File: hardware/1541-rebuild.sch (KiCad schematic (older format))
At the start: 1 part

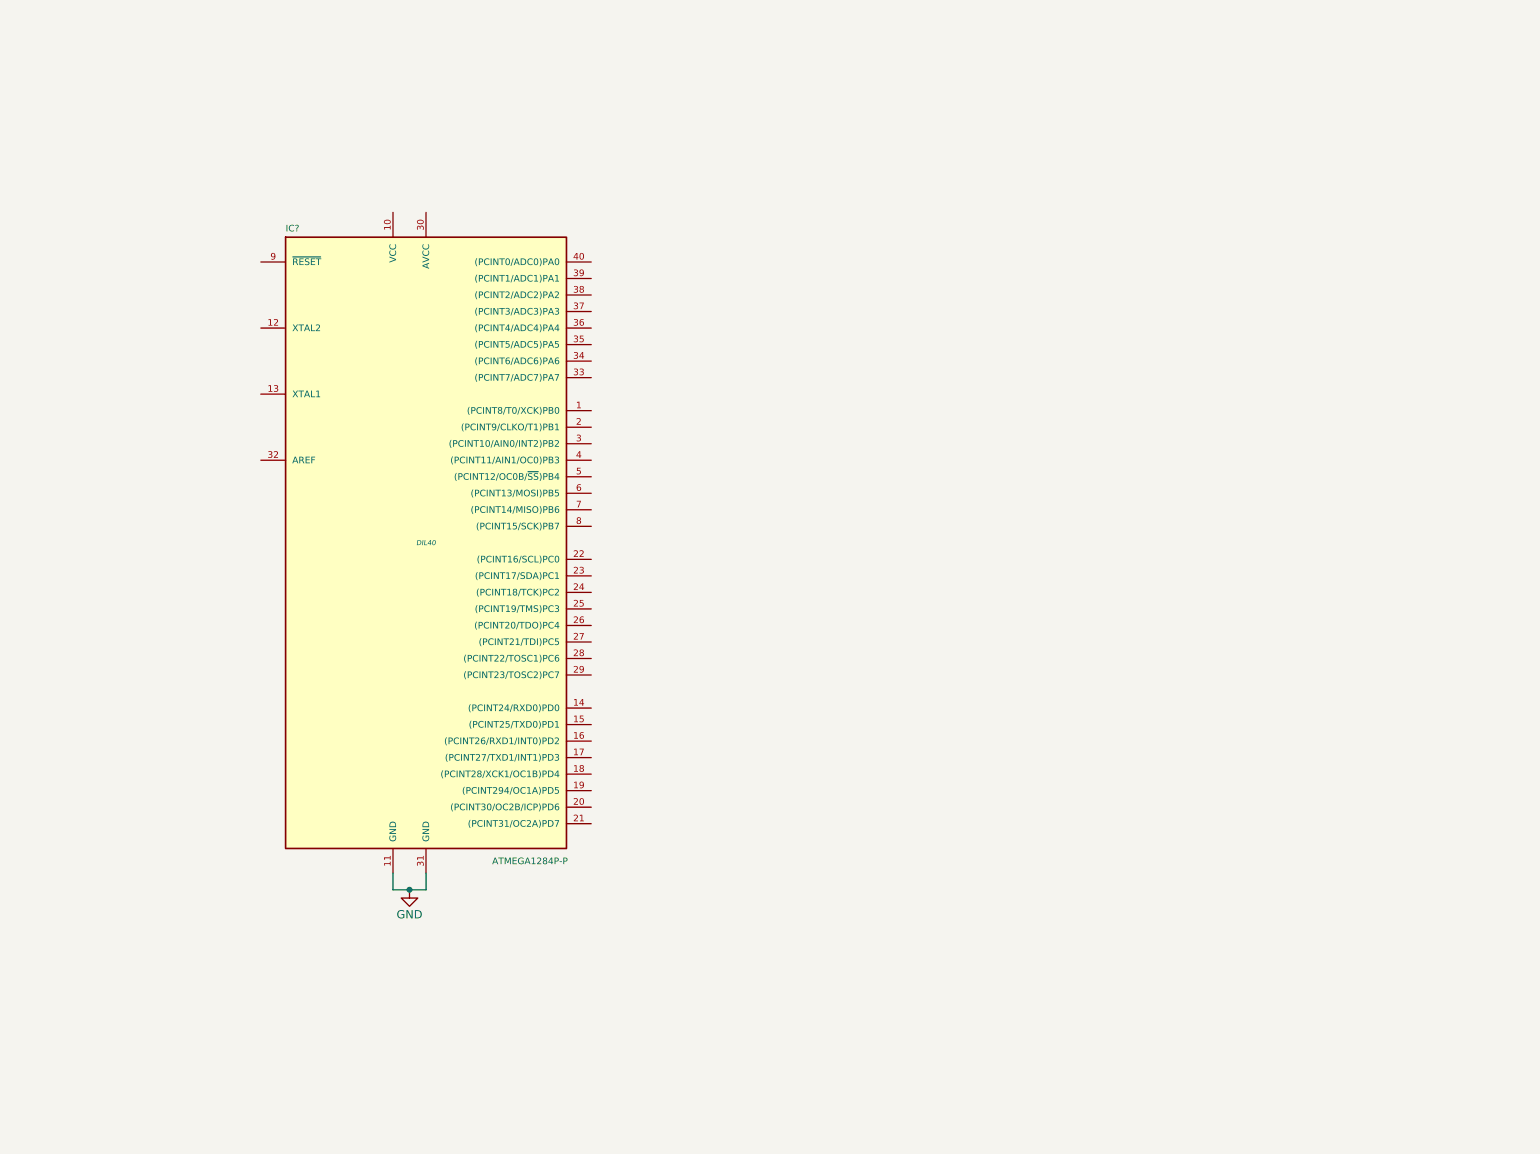
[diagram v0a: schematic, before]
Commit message: Im Schaltplan die SD Karten Anbindung eingefügt
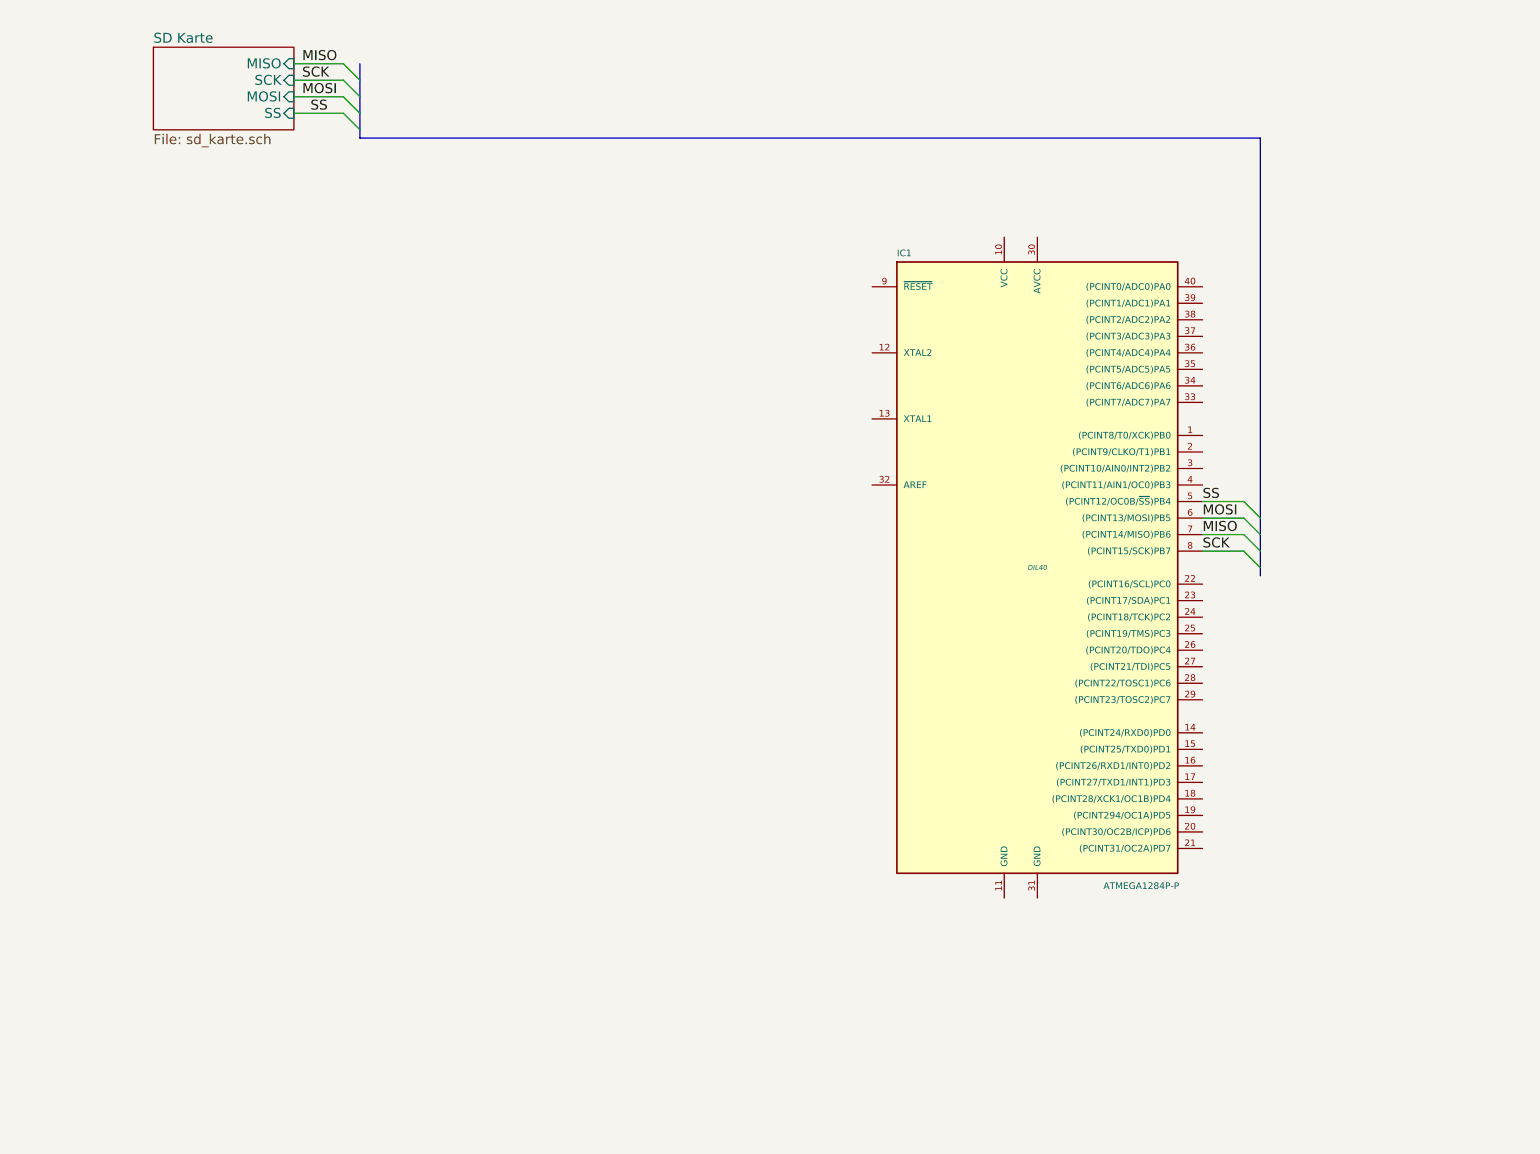
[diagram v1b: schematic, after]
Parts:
- removed IC?: ATMEGA1284P-P, DIL40, symbol ATMEGA1284P-P
- added IC1: ATMEGA1284P-P, DIL40, symbol ATMEGA1284P-P
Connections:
- new net MISO: IC1.7 ((PCINT14/MISO)PB6)
- new net MOSI: IC1.6 ((PCINT13/MOSI)PB5)
- new net SCK: IC1.8 ((PCINT15/SCK)PB7)
- new net SS: IC1.5 ((PCINT12/OC0B/~SS~)PB4)
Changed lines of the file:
@@
 LIBS:contrib
 LIBS:valves
+LIBS:1541-rebuild-cache
 EELAYER 25 0
 EELAYER END
 $Descr A4 11693 8268
 encoding utf-8
-Sheet 1 1
-Title ""
-Date ""
-Rev ""
+Sheet 1 2
+Title "1541-rebuild"
+Date "2015-09-15"
+Rev "1.0"
 Comp ""
-Comment1 ""
+Comment1 "Erstellt: von: Thorsten Kattanek"
 Comment2 ""
 Comment3 ""
 Comment4 ""
 $EndDescr
+$Sheet
+S 1500 850  850  500
+U 55F7A0F9
+F0 "SD Karte" 60
+F1 "sd_karte.sch" 60
+F2 "MISO" I R 2350 950 60
+F3 "SCK" I R 2350 1050 60
+F4 "MOSI" I R 2350 1150 60
+F5 "SS" I R 2350 1250 60
+$EndSheet
 $Comp
-L ATMEGA1284P-P IC?
-U 1 1 55F6F7E1
-P 3150 3850
-F 0 "IC?" H 2300 5730 40  0000 L BNN
-F 1 "ATMEGA1284P-P" H 3550 1900 40  0000 L BNN
-F 2 "DIL40" H 3150 3850 30  0000 C CIN
-F 3 "" H 3150 3850 60  0000 C CNN
-	1    3150 3850
+L ATMEGA1284P-P IC1
+U 1 1 55F7E447
+P 6850 4000
+F 0 "IC1" H 6000 5880 40  0000 L BNN
+F 1 "ATMEGA1284P-P" H 7250 2050 40  0000 L BNN
+F 2 "DIL40" H 6850 4000 30  0000 C CIN
+F 3 "" H 6850 4000 60  0000 C CNN
+	1    6850 4000
 	1    0    0    -1
 $EndComp
-$Comp
-L GND #PWR?
-U 1 1 55F6F9CF
-P 3050 5950
-F 0 "#PWR?" H 3050 5700 50  0001 C CNN
-F 1 "GND" H 3050 5800 50  0000 C CNN
-F 2 "" H 3050 5950 60  0000 C CNN
-F 3 "" H 3050 5950 60  0000 C CNN
-	1    3050 5950
-	1    0    0    -1
-$EndComp
+Wire Bus Line
+	2750 950  2750 1400
+Wire Bus Line
+	2750 1400 8200 1400
+Wire Bus Line
+	8200 1400 8200 4050
+Entry Wire Line
+	2650 950  2750 1050
+Entry Wire Line
+	2650 1050 2750 1150
+Entry Wire Line
+	2650 1150 2750 1250
+Entry Wire Line
+	2650 1250 2750 1350
 Wire Wire Line
-	2950 5850 2950 5950
+	2650 950  2350 950
 Wire Wire Line
-	2950 5950 3050 5950
+	2650 1050 2350 1050
 Wire Wire Line
-	3050 5950 3150 5950
+	2650 1150 2350 1150
 Wire Wire Line
-	3150 5950 3150 5850
-Connection ~ 3050 5950
+	2650 1250 2350 1250
+Text Label 2400 950  0    60   ~ 0
+MISO
+Text Label 2400 1050 0    60   ~ 0
+SCK
+Text Label 2400 1150 0    60   ~ 0
+MOSI
+Text Label 2450 1250 0    60   ~ 0
+SS
+Entry Wire Line
+	8100 3600 8200 3700
+Entry Wire Line
+	8100 3700 8200 3800
+Entry Wire Line
+	8100 3800 8200 3900
+Entry Wire Line
+	8100 3900 8200 4000
+Wire Wire Line
+	7850 3600 8100 3600
+Wire Wire Line
+	7850 3700 8100 3700
+Wire Wire Line
+	7850 3800 8100 3800
+Wire Wire Line
+	7850 3900 8100 3900
+Text Label 7850 3600 0    60   ~ 0
+SS
+Text Label 7850 3700 0    60   ~ 0
+MOSI
+Text Label 7850 3800 0    60   ~ 0
+MISO
+Text Label 7850 3900 0    60   ~ 0
+SCK
 $EndSCHEMATC

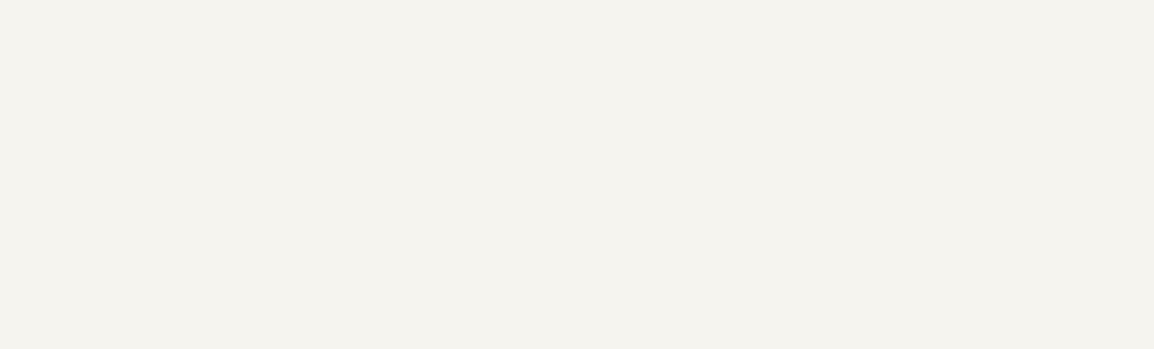
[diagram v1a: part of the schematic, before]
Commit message: Hinweistext zur Modifikation der 1541 Platine hinzugefügt
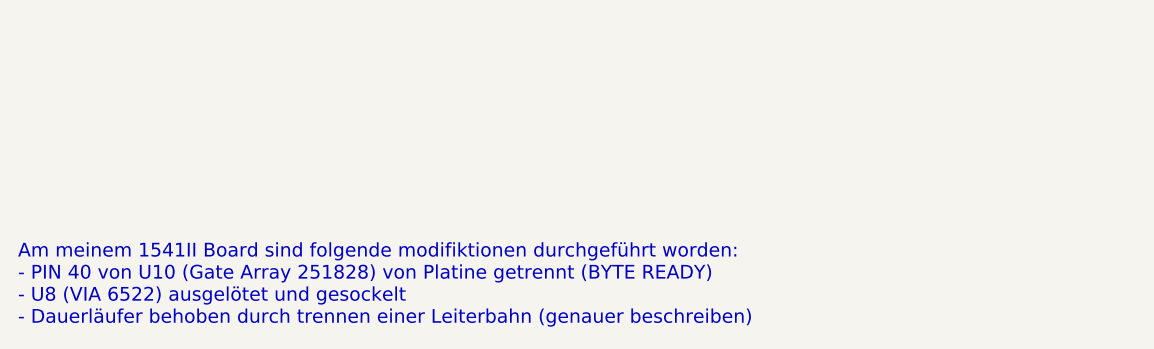
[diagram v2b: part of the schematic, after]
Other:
- note added: "Am meinem 1541II Board sind folgende modifiktionen durchgeführt worden:\n- PIN 40 von U10 (Gate Array 251828) von Platine getrennt (BYTE READY)\n- U8 (VIA 6522) ausgelötet und gesockelt\n- Dauerläufer behoben durch trennen einer Leiterbahn (genauer beschreiben)"
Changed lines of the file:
@@
 Text Label 7850 3900 0    60   ~ 0
 SCK
+Text Notes 650  7450 0    60   ~ 0
+Am meinem 1541II Board sind folgende modifiktionen durchgeführt worden:\n- PIN 40 von U10 (Gate Array 251828) von Platine getrennt (BYTE READY)\n- U8 (VIA 6522) ausgelötet und gesockelt\n- Dauerläufer behoben durch trennen einer Leiterbahn (genauer beschreiben)
 $EndSCHEMATC

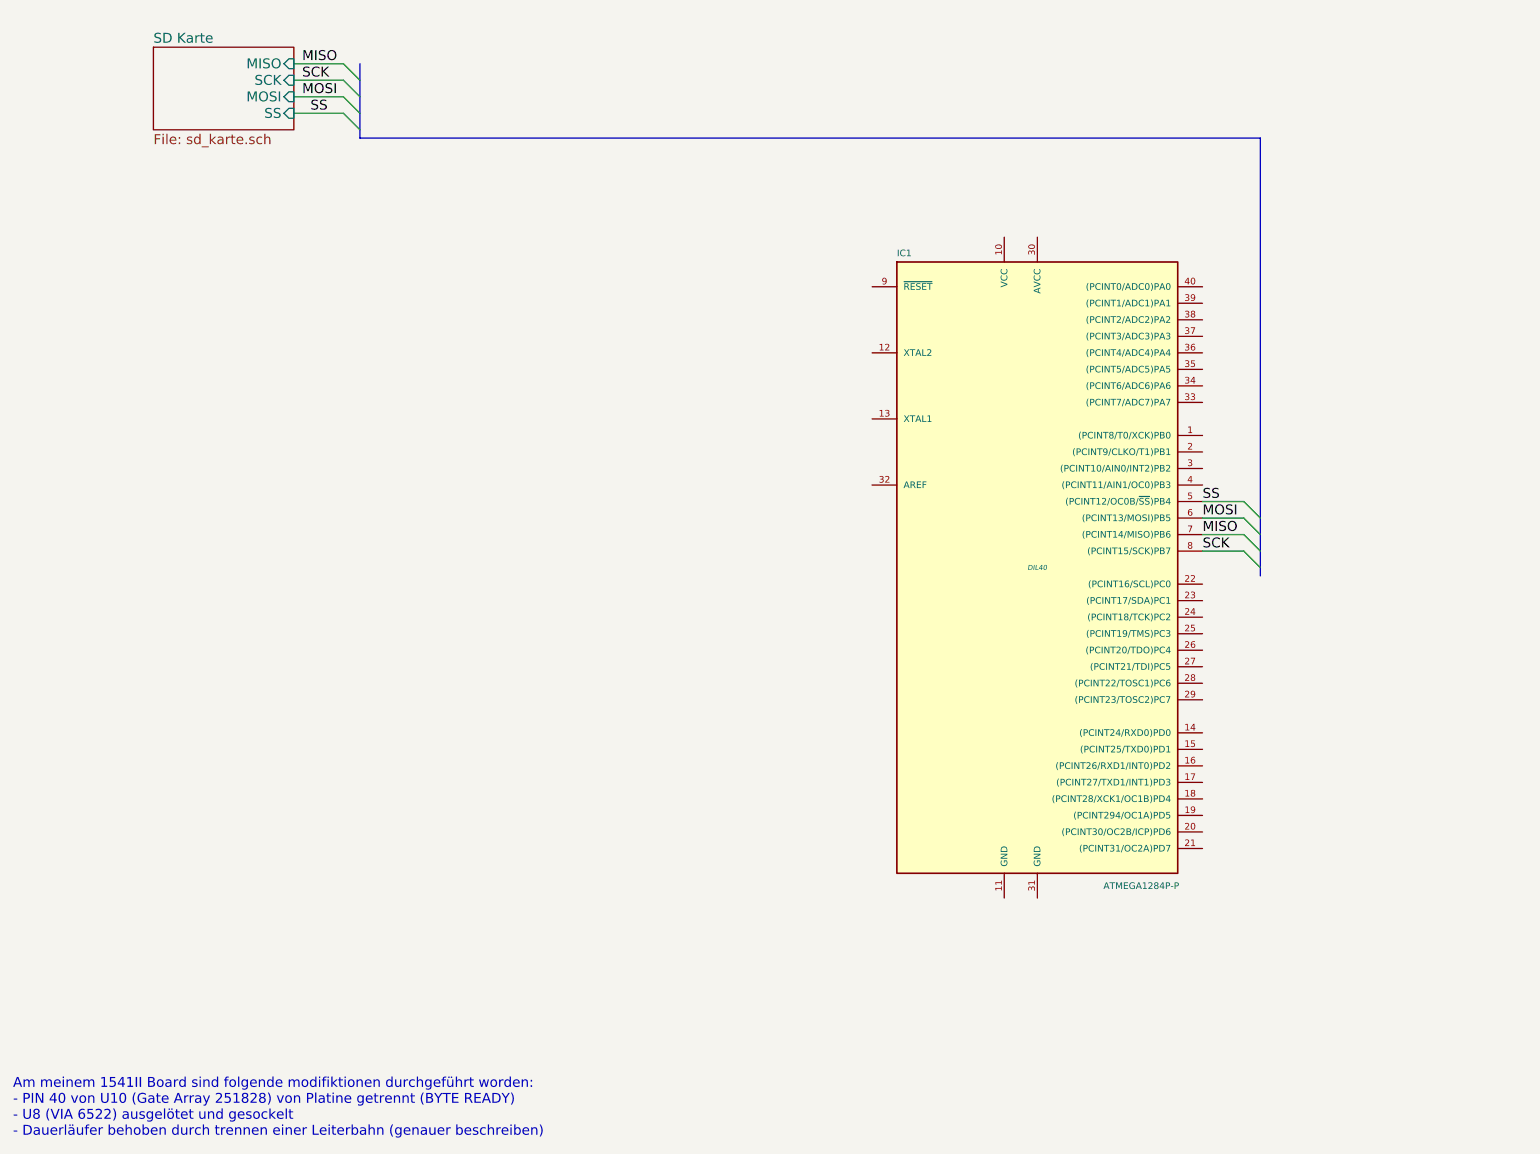
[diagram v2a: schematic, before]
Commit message: .bak Dateien aus Repo entfernt.Qscillator im Schaltpan hinzugefügt
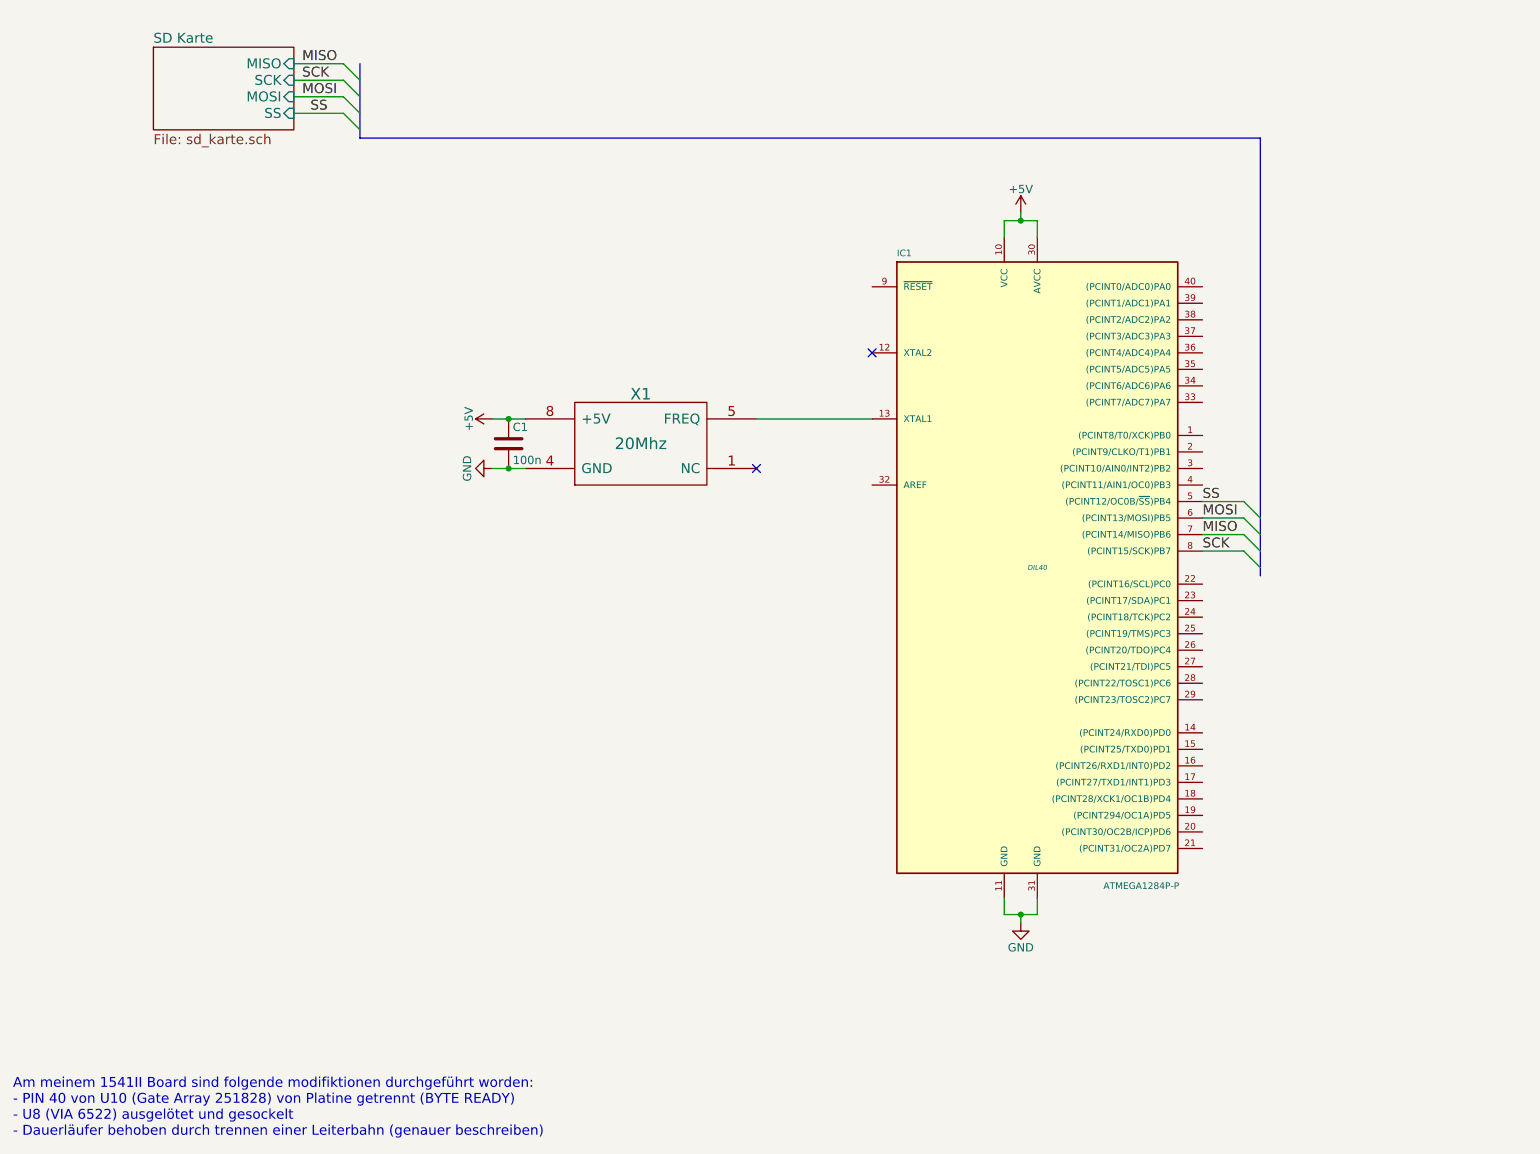
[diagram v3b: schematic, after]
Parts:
- added C1: 100n, symbol C
- added X1: 20Mhz, symbol TCXO3
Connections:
- net +5V: now reaches IC1.10 (VCC)
- net +5V: now also IC1.30 (AVCC), C1.1, X1.8 (+5V)
- net GND: now reaches IC1.11 (GND)
- net GND: now also IC1.31 (GND), C1.2, X1.4 (GND)
- net at IC1.13 (XTAL1): now also X1.5 (FREQ)
- no-connect marks 0 -> 2
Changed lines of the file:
@@
 LIBS:contrib
 LIBS:valves
+LIBS:Oscillators
 LIBS:1541-rebuild-cache
 EELAYER 25 0
@@
 Text Notes 650  7450 0    60   ~ 0
 Am meinem 1541II Board sind folgende modifiktionen durchgeführt worden:\n- PIN 40 von U10 (Gate Array 251828) von Platine getrennt (BYTE READY)\n- U8 (VIA 6522) ausgelötet und gesockelt\n- Dauerläufer behoben durch trennen einer Leiterbahn (genauer beschreiben)
+$Comp
+L TCXO3 X1
+U 1 1 55F7CB9E
+P 4450 3250
+F 0 "X1" H 4450 3550 70  0000 C CNN
+F 1 "20Mhz" H 4450 3250 70  0000 C CNN
+F 2 "" H 4450 3250 60  0000 C CNN
+F 3 "" H 4450 3250 60  0000 C CNN
+	1    4450 3250
+	1    0    0    -1
+$EndComp
+Wire Wire Line
+	5150 3100 5850 3100
+NoConn ~ 5150 3400
+$Comp
+L GND #PWR2
+U 1 1 55F7D4A6
+P 3550 3400
+F 0 "#PWR2" H 3550 3150 50  0001 C CNN
+F 1 "GND" H 3550 3250 50  0000 C CNN
+F 2 "" H 3550 3400 60  0000 C CNN
+F 3 "" H 3550 3400 60  0000 C CNN
+	1    3550 3400
+	0    1    1    0
+$EndComp
+$Comp
+L +5V #PWR1
+U 1 1 55F7D4E4
+P 3550 3100
+F 0 "#PWR1" H 3550 2950 50  0001 C CNN
+F 1 "+5V" H 3550 3240 50  0000 C CNN
+F 2 "" H 3550 3100 60  0000 C CNN
+F 3 "" H 3550 3100 60  0000 C CNN
+	1    3550 3100
+	0    -1   -1   0
+$EndComp
+$Comp
+L C C1
+U 1 1 55F7D642
+P 3650 3250
+F 0 "C1" H 3675 3350 50  0000 L CNN
+F 1 "100n" H 3675 3150 50  0000 L CNN
+F 2 "" H 3688 3100 30  0000 C CNN
+F 3 "" H 3650 3250 60  0000 C CNN
+	1    3650 3250
+	1    0    0    -1
+$EndComp
+Wire Wire Line
+	3550 3100 3750 3100
+Connection ~ 3650 3100
+Wire Wire Line
+	3550 3400 3750 3400
+Connection ~ 3650 3400
+NoConn ~ 5850 2700
+$Comp
+L GND #PWR?
+U 1 1 55F7EFD4
+P 6750 6150
+F 0 "#PWR?" H 6750 5900 50  0001 C CNN
+F 1 "GND" H 6750 6000 50  0000 C CNN
+F 2 "" H 6750 6150 60  0000 C CNN
+F 3 "" H 6750 6150 60  0000 C CNN
+	1    6750 6150
+	1    0    0    -1
+$EndComp
+Wire Wire Line
+	6650 6000 6650 6100
+Wire Wire Line
+	6650 6100 6850 6100
+Wire Wire Line
+	6750 6100 6750 6150
+Wire Wire Line
+	6850 6100 6850 6000
+Connection ~ 6750 6100
+$Comp
+L +5V #PWR?
+U 1 1 55F7F7C2
+P 6750 1850
+F 0 "#PWR?" H 6750 1700 50  0001 C CNN
+F 1 "+5V" H 6750 1990 50  0000 C CNN
+F 2 "" H 6750 1850 60  0000 C CNN
+F 3 "" H 6750 1850 60  0000 C CNN
+	1    6750 1850
+	1    0    0    -1
+$EndComp
+Wire Wire Line
+	6650 2000 6650 1900
+Wire Wire Line
+	6650 1900 6850 1900
+Wire Wire Line
+	6750 1900 6750 1850
+Wire Wire Line
+	6850 1900 6850 2000
+Connection ~ 6750 1900
 $EndSCHEMATC
